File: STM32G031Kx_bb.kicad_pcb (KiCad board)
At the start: 2 copper layers, 17.8 x 38.1 mm, 16 parts, among them J1 GPIO1, J2 GPIO2, SW1 Reset, U1 STM32G031Kx, U2 AP2210, Y1 LSE

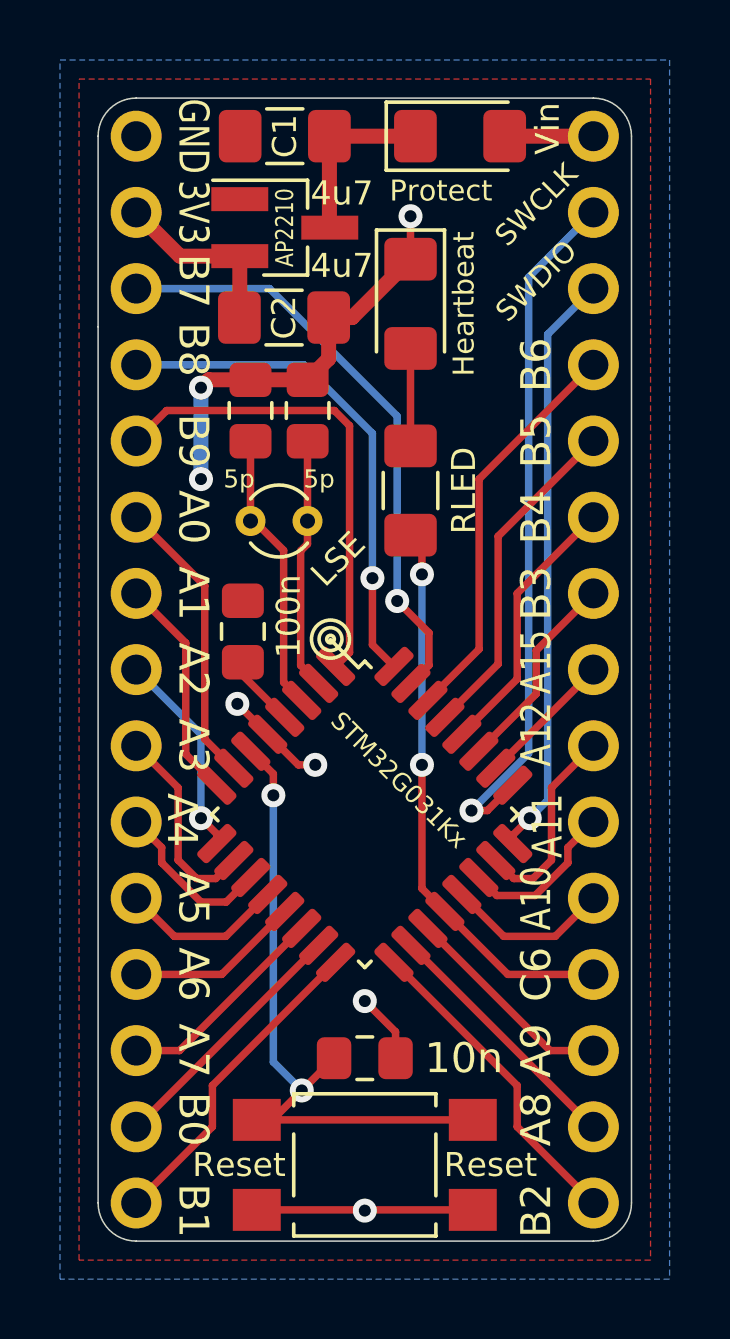
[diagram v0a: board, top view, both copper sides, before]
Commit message: Connect the MCU power supply to the voltage regulator's output...whoops!
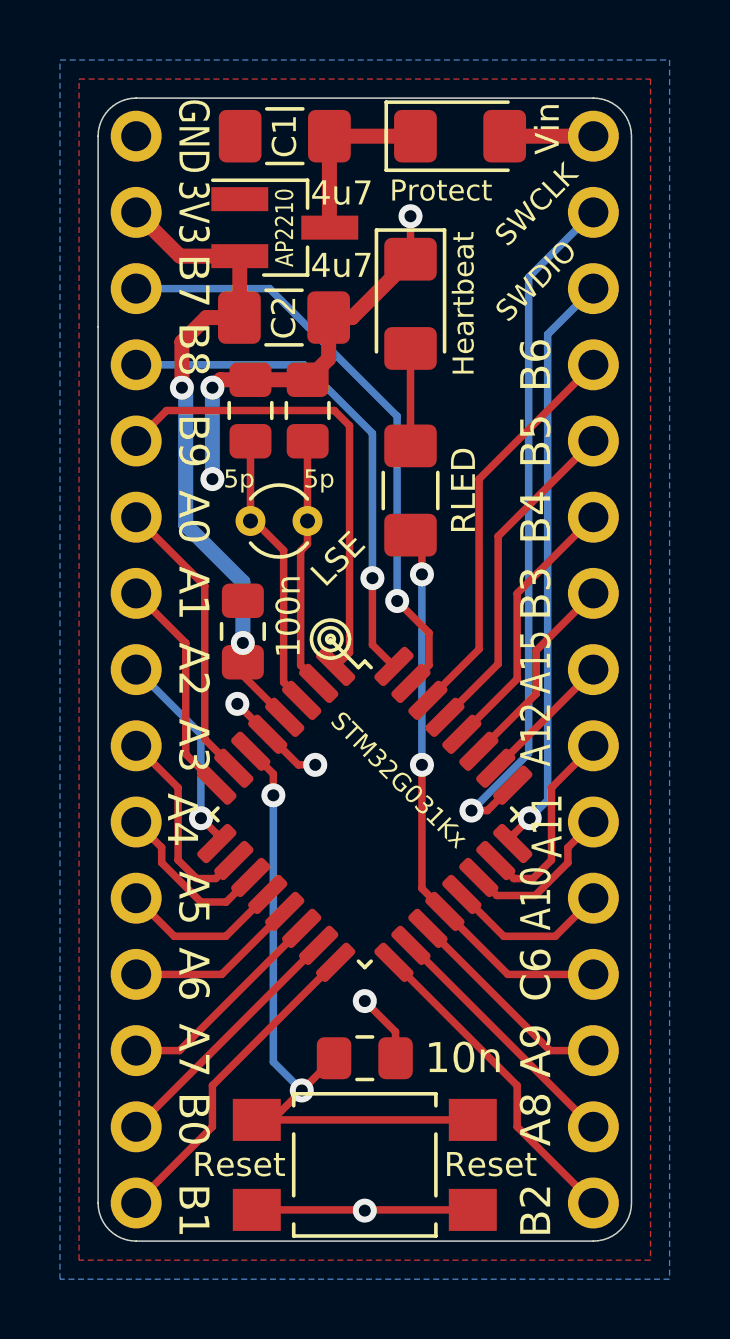
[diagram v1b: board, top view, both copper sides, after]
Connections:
- C5 pad 1: Net-(C5-Pad1) -> VDD
- U1 pad 4: Net-(C5-Pad1) -> VDD
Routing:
- net VDD: track 6.11 -> 22.3 mm, vias 0 -> 2
- net Net-(C5-Pad1): track 2.41 -> 0.00 mm
